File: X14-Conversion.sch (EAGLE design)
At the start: 13 parts, among them U1 LM2678SX-ADJ/NOPBTS7B

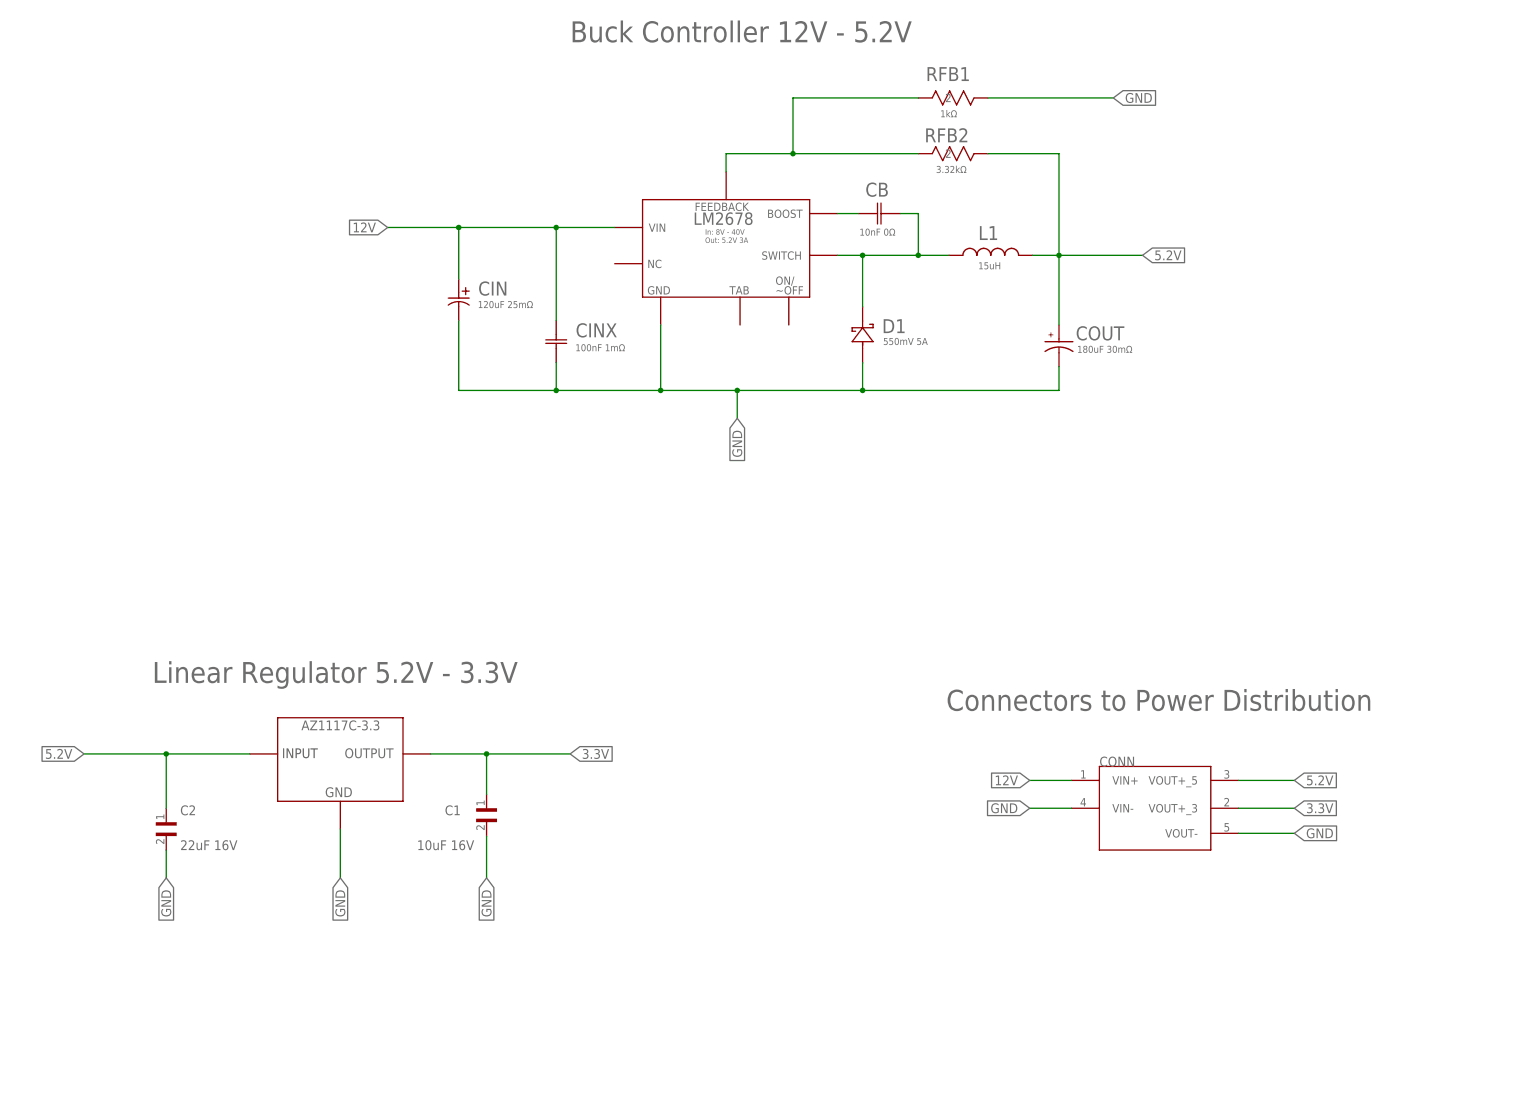
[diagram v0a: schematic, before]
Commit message: Fix Schematic, add test points, screw terminals and connectors
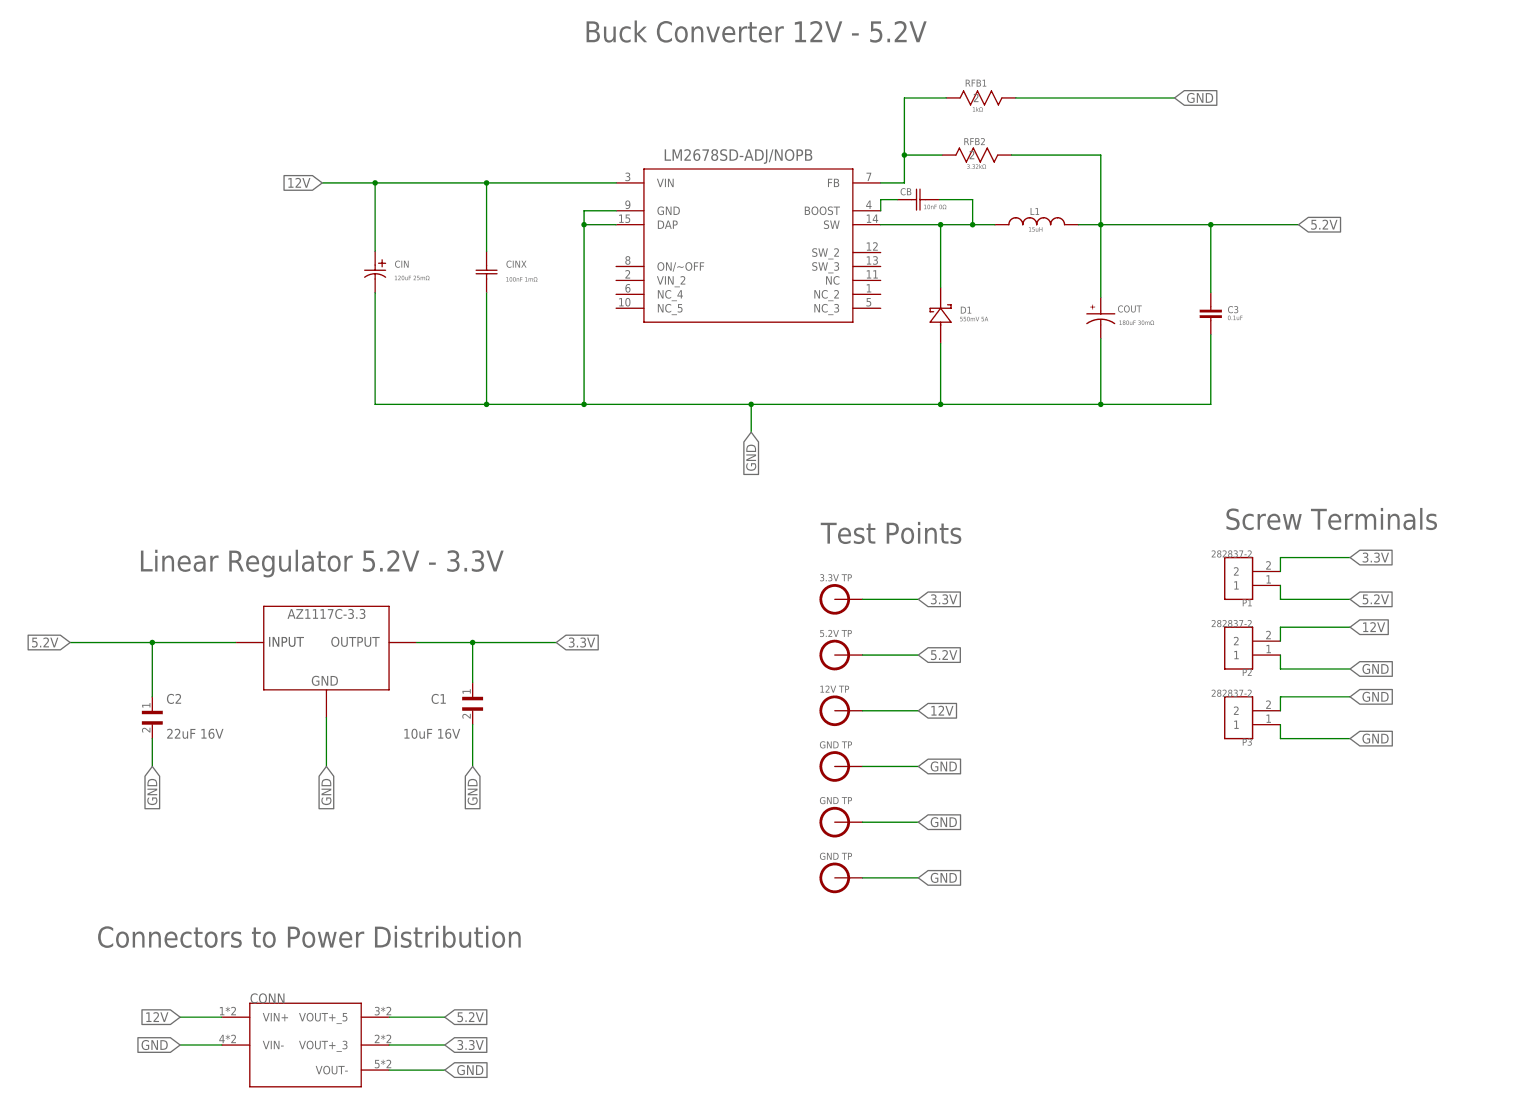
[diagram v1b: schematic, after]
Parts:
- removed U1: LM2678SX-ADJ/NOPBTS7B, LM2678SX-ADJNOPB:LM2678SX-ADJ/NOPBTS7B
- added C3: 0.1uF, SparkFun-Capacitors:0.1UF-0402-16V-10%
- added P1, P2, P3: 282837-2, ScrewPoints_282837-2:282837-2
- added U$2: 3.3V_TESTPOINT, testpoints:3.3V_TESTPOINT
- added U$3: 5.2V_TESTPOINT, testpoints:5.2V_TESTPOINT
- added U$4: 12V_TESTPOINT, testpoints:12V_TESTPOINT
- added U$5, U$6, U$7: GND_TESTPOINT, testpoints:GND_TESTPOINT
- added U2: LM2678SD-ADJ/NOPB, LM2678SX-ADJNOPB:LM2678SD-ADJ/NOPB
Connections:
- removed net N$1: RFB1.2, RFB2.2, U1.FEEDBACK
- removed net N$3: CB.2, D1.1, L1.1, U1.SWITCH_OUTPUT
- new net N$4: CB.1, U2.BOOST
- new net N$5: RFB1.2, RFB2.2, U2.FB
- net 12V: now also P2.2, U$4.12V, U2.VIN; no longer U1.VIN
- net 3.3V: now also P1.2, U$2.3.3V
- net 5.2V: now also C3.1, P1.1, U$3.5.2V
- net GND: now also C3.2, P2.1, P3.1, P3.2, U$5.GND, U$6.GND, U$7.GND, U2.DAP, U2.GND; no longer U1.GND
- net N$2: now also CB.2, D1.1, L1.1, U2.SW; no longer CB.1, U1.CB
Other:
- note added: "Buck Converter 12V - 5.2V"
- note added: "Screw Terminals"
- note added: "Test Points"
- note removed: "Buck Controller 12V - 5.2V"
- moved on the sheet: C1, C2, CB, CIN, CINX, CONN, COUT, D1, L1, RFB1, RFB2

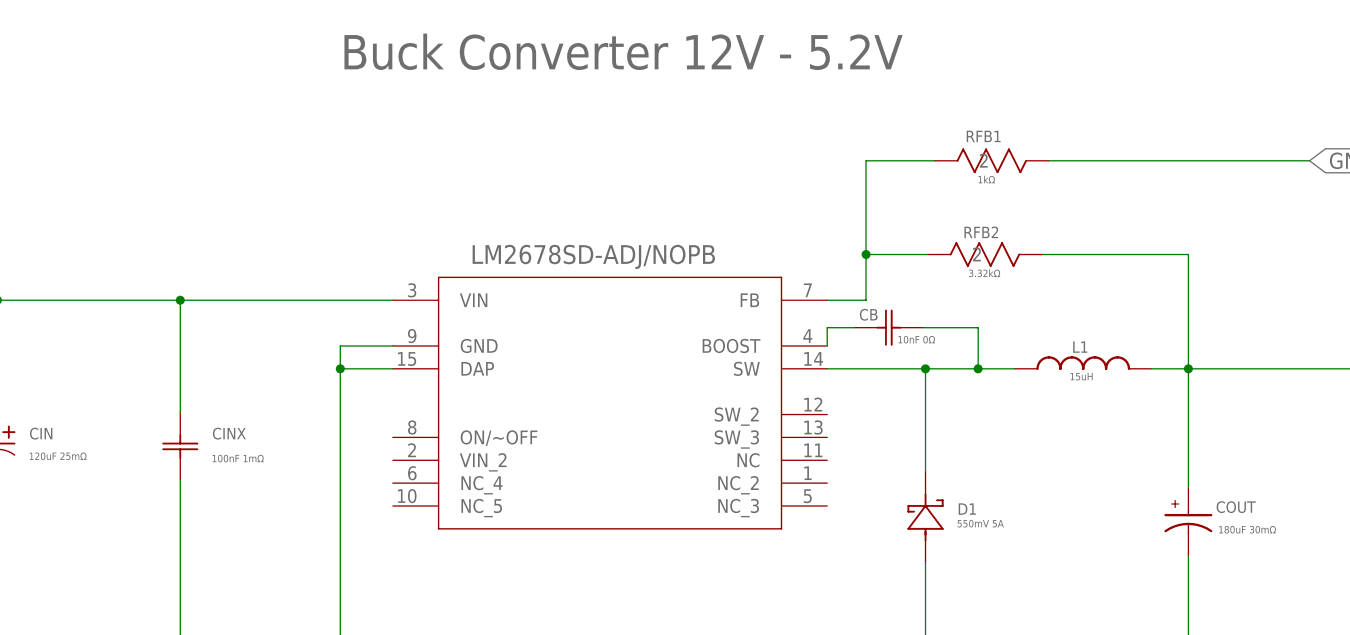
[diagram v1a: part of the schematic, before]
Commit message: Fix capacitors and resistors to Sparkfun components
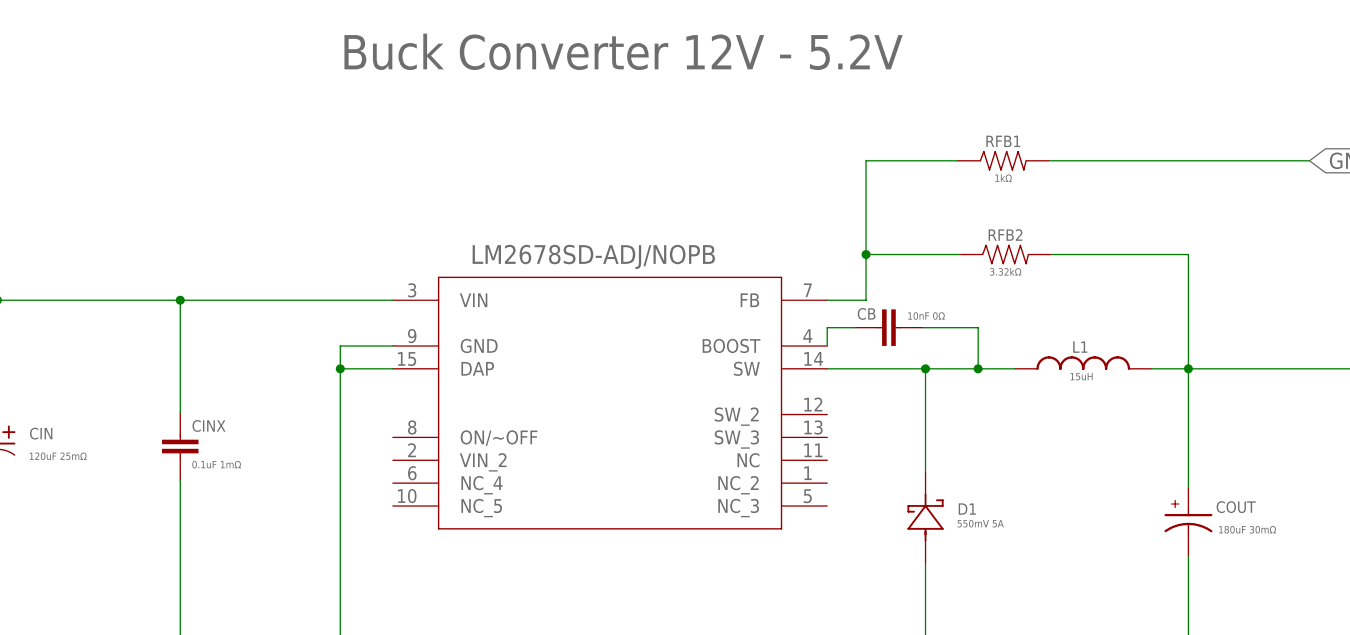
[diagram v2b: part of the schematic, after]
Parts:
- CB: device CGA4C2C0G1H103J060AA:CGA4C2C0G1H103J060AACAP_2012_TDK -> SparkFun-Capacitors:10NF-0603-50V-10%
- CINX: value 100nF 1mΩ -> 0.1uF 1mΩ; device GRM155R71C104KA88D:GRM155R71C104KA88DCAP_GRM_155_MUR -> SparkFun-Capacitors:0.1UF-0603-25V-(+80/-20%)
- RFB1: device CRCW04021K00FKED:CRCW04021K00FKEDRES_CRCW_0402 -> SparkFun-Resistors:1KOHM-0603-1/10W-1%
- RFB2: device CRCW04023K32FKED:CRCW04023K32FKEDRES_CRCW_0402 -> SparkFun-Resistors:3.3KOHM-0603-1/10W-1%
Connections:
- net 5.2V: now also RFB2.2; no longer RFB2.1
- net GND: now also RFB1.2; no longer RFB1.1
- net N$5: now also RFB1.1, RFB2.1; no longer RFB1.2, RFB2.2
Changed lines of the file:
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@@
 </classes>
 <parts>
-<part name="RFB1" library="CRCW04021K00FKED" deviceset="CRCW04021K00FKED" device="RES_CRCW_0402" value="1kΩ"/>
 <part name="D1" library="CDBC520-G_Library" deviceset="CDBC520-G" device="CDBC-G" value="550mV 5A"/>
 <part name="CIN" library="20SVPF120M" deviceset="20SVPF120M" device="PCAP_SVP_C6_PAN" value="120uF 25mΩ"/>
-<part name="RFB2" library="CRCW04023K32FKED" deviceset="CRCW04023K32FKED" device="RES_CRCW_0402" value="3.32kΩ"/>
 <part name="L1" library="IND, 15uH - hcma1305" deviceset="HCMA1305" device="" package3d_urn="urn:adsk.eagle:package:24201702/2" value="15uH"/>
-<part name="CB" library="CGA4C2C0G1H103J060AA" deviceset="CGA4C2C0G1H103J060AA" device="CAP_2012_TDK" value="10nF 0Ω"/>
 <part name="COUT" library="16SVP180MX" deviceset="16SVP180MX" device="" value="180uF 30mΩ"/>
-<part name="CINX" library="GRM155R71C104KA88D" deviceset="GRM155R71C104KA88D" device="CAP_GRM_155_MUR" value="100nF 1mΩ"/>
 <part name="FRAME1" library="frames" library_urn="urn:adsk.eagle:library:229" deviceset="A3L-LOC" device=""/>
 <part name="U$1" library="AZ1117C-3.3" deviceset="SOT150P410X160-3N" device=""/>
@@
 <part name="P3" library="ScrewPoints_282837-2" deviceset="282837-2" device=""/>
 <part name="C3" library="SparkFun-Capacitors" library_urn="urn:adsk.eagle:library:510" deviceset="0.1UF" device="-0402-16V-10%" package3d_urn="urn:adsk.eagle:package:37413/1" value="0.1uF"/>
+<part name="RFB2" library="SparkFun-Resistors" library_urn="urn:adsk.eagle:library:532" deviceset="3.3KOHM" device="-0603-1/10W-1%" package3d_urn="urn:adsk.eagle:package:39650/1" value="3.32kΩ"/>
+<part name="RFB1" library="SparkFun-Resistors" library_urn="urn:adsk.eagle:library:532" deviceset="1KOHM" device="-0603-1/10W-1%" package3d_urn="urn:adsk.eagle:package:39650/1" value="1kΩ"/>
+<part name="CB" library="SparkFun-Capacitors" library_urn="urn:adsk.eagle:library:510" deviceset="10NF" device="-0603-50V-10%" package3d_urn="urn:adsk.eagle:package:37414/1" value="10nF 0Ω"/>
+<part name="CINX" library="SparkFun-Capacitors" library_urn="urn:adsk.eagle:library:510" deviceset="0.1UF" device="-0603-25V-(+80/-20%)" package3d_urn="urn:adsk.eagle:package:37414/1" value="0.1uF 1mΩ"/>
 </parts>
 <sheets>
@@
 </plain>
 <instances>
-<instance part="RFB1" gate="A" x="38.1" y="88.9" smashed="yes">
-<attribute name="VALUE" x="42.8529" y="86.3981" size="0.8128" layer="96" ratio="10"/>
-<attribute name="NAME" x="41.5082" y="90.9701" size="1.27" layer="95" ratio="10"/>
-</instance>
 <instance part="D1" gate="A" x="37.084" y="54.356" smashed="yes" rot="R270">
 <attribute name="VALUE" x="40.5669" y="48.1711" size="0.8128" layer="96" ratio="10"/>
@@
 <attribute name="NAME" x="-62.5048" y="57.9501" size="1.27" layer="95" ratio="10"/>
 </instance>
-<instance part="RFB2" gate="A" x="37.338" y="78.486" smashed="yes">
-<attribute name="VALUE" x="41.8369" y="75.9841" size="0.8128" layer="96" ratio="10"/>
-<attribute name="NAME" x="41.2542" y="80.3021" size="1.27" layer="95" ratio="10"/>
-</instance>
 <instance part="L1" gate="G$1" x="46.99" y="65.786" smashed="yes">
 <attribute name="NAME" x="53.34" y="67.564" size="1.27" layer="95"/>
 <attribute name="VALUE" x="53.086" y="64.516" size="0.8128" layer="96"/>
 </instance>
-<instance part="CB" gate="A" x="29.21" y="70.358" smashed="yes">
-<attribute name="VALUE" x="33.9629" y="68.6181" size="0.8128" layer="96" ratio="10"/>
-<attribute name="NAME" x="29.6972" y="71.1581" size="1.27" layer="95" ratio="10"/>
-</instance>
 <instance part="COUT" gate="G$1" x="66.294" y="50.038" smashed="yes" rot="R270">
 <attribute name="NAME" x="69.342" y="49.784" size="1.27" layer="95"/>
 <attribute name="VALUE" x="69.596" y="47.498" size="0.8128" layer="96"/>
-</instance>
-<instance part="CINX" gate="A" x="-45.72" y="60.96" smashed="yes" rot="R270">
-<attribute name="VALUE" x="-42.2371" y="55.4101" size="0.8128" layer="96" ratio="10"/>
-<attribute name="NAME" x="-42.1848" y="57.9501" size="1.27" layer="95" ratio="10"/>
 </instance>
 <instance part="FRAME1" gate="G$1" x="-177.8" y="-116.84" smashed="yes">
@@
 <attribute name="VALUE" x="89.408" y="48.387" size="0.8128" layer="96"/>
 </instance>
+<instance part="RFB2" gate="G$1" x="45.974" y="78.486" smashed="yes">
+<attribute name="NAME" x="45.974" y="80.01" size="1.27" layer="95" align="bottom-center"/>
+<attribute name="VALUE" x="45.974" y="76.962" size="0.8128" layer="96" align="top-center"/>
+</instance>
+<instance part="RFB1" gate="G$1" x="45.72" y="88.9" smashed="yes">
+<attribute name="NAME" x="45.72" y="90.424" size="1.27" layer="95" align="bottom-center"/>
+<attribute name="VALUE" x="45.72" y="87.376" size="0.8128" layer="96" align="top-center"/>
+</instance>
+<instance part="CB" gate="G$1" x="34.29" y="70.358" smashed="yes" rot="R90">
+<attribute name="NAME" x="29.464" y="71.247" size="1.27" layer="95"/>
+<attribute name="VALUE" x="35.052" y="71.247" size="0.8128" layer="96"/>
+</instance>
+<instance part="CINX" gate="G$1" x="-45.72" y="55.88" smashed="yes">
+<attribute name="NAME" x="-44.45" y="58.801" size="1.27" layer="95"/>
+<attribute name="VALUE" x="-44.45" y="54.737" size="0.8128" layer="96"/>
+</instance>
 </instances>
 <busses>
@@
 <pinref part="COUT" gate="G$1" pin="2"/>
 <wire x1="66.294" y1="44.958" x2="66.294" y2="33.02" width="0.1524" layer="91"/>
-<pinref part="CINX" gate="A" pin="2"/>
 <wire x1="-45.72" y1="53.34" x2="-45.72" y2="33.02" width="0.1524" layer="91"/>
 <wire x1="-45.72" y1="33.02" x2="-27.94" y2="33.02" width="0.1524" layer="91"/>
@@
 <wire x1="86.36" y1="33.02" x2="86.36" y2="45.72" width="0.1524" layer="91"/>
 <junction x="66.294" y="33.02"/>
-</segment>
-<segment>
-<pinref part="RFB1" gate="A" pin="1"/>
+<pinref part="CINX" gate="G$1" pin="2"/>
+</segment>
+<segment>
 <wire x1="50.8" y1="88.9" x2="79.756" y2="88.9" width="0.1524" layer="91"/>
 <label x="79.756" y="88.9" size="1.778" layer="95" xref="yes"/>
+<pinref part="RFB1" gate="G$1" pin="2"/>
 </segment>
 <segment>
@@
 <pinref part="COUT" gate="G$1" pin="1"/>
 <wire x1="66.294" y1="52.578" x2="66.294" y2="65.786" width="0.1524" layer="91"/>
-<pinref part="RFB2" gate="A" pin="1"/>
-<wire x1="50.038" y1="78.486" x2="66.294" y2="78.486" width="0.1524" layer="91"/>
+<wire x1="51.054" y1="78.486" x2="66.294" y2="78.486" width="0.1524" layer="91"/>
 <wire x1="66.294" y1="78.486" x2="66.294" y2="65.786" width="0.1524" layer="91"/>
 <junction x="66.294" y="65.786"/>
@@
 <wire x1="86.36" y1="53.34" x2="86.36" y2="65.786" width="0.1524" layer="91"/>
 <junction x="86.36" y="65.786"/>
+<pinref part="RFB2" gate="G$1" pin="2"/>
 </segment>
 <segment>
@@
 <segment>
 <pinref part="U2" gate="A" pin="VIN"/>
-<pinref part="CINX" gate="A" pin="1"/>
 <wire x1="-22.098" y1="73.406" x2="-45.72" y2="73.406" width="0.1524" layer="91"/>
 <wire x1="-45.72" y1="73.406" x2="-45.72" y2="60.96" width="0.1524" layer="91"/>
@@
 <junction x="-66.04" y="73.406"/>
 <label x="-75.692" y="73.406" size="1.778" layer="95" rot="R180" xref="yes"/>
+<pinref part="CINX" gate="G$1" pin="1"/>
 </segment>
 <segment>
@@
 <pinref part="L1" gate="G$1" pin="1"/>
 <wire x1="26.162" y1="65.786" x2="37.084" y2="65.786" width="0.1524" layer="91"/>
-<pinref part="CB" gate="A" pin="2"/>
 <wire x1="37.084" y1="65.786" x2="42.926" y2="65.786" width="0.1524" layer="91"/>
 <wire x1="42.926" y1="65.786" x2="46.99" y2="65.786" width="0.1524" layer="91"/>
@@
 <wire x1="37.084" y1="54.356" x2="37.084" y2="65.786" width="0.1524" layer="91"/>
 <junction x="37.084" y="65.786"/>
+<pinref part="CB" gate="G$1" pin="2"/>
 </segment>
 </net>
@@
 <segment>
 <pinref part="U2" gate="A" pin="BOOST"/>
-<pinref part="CB" gate="A" pin="1"/>
 <wire x1="26.162" y1="68.326" x2="26.162" y2="70.358" width="0.1524" layer="91"/>
 <wire x1="26.162" y1="70.358" x2="29.21" y2="70.358" width="0.1524" layer="91"/>
+<pinref part="CB" gate="G$1" pin="1"/>
 </segment>
 </net>
@@
 <wire x1="26.162" y1="73.406" x2="30.48" y2="73.406" width="0.1524" layer="91"/>
 <wire x1="30.48" y1="73.406" x2="30.48" y2="78.486" width="0.1524" layer="91"/>
-<pinref part="RFB2" gate="A" pin="2"/>
-<wire x1="30.48" y1="78.486" x2="37.338" y2="78.486" width="0.1524" layer="91"/>
-<pinref part="RFB1" gate="A" pin="2"/>
+<wire x1="30.48" y1="78.486" x2="40.894" y2="78.486" width="0.1524" layer="91"/>
 <wire x1="30.48" y1="78.486" x2="30.48" y2="88.9" width="0.1524" layer="91"/>
-<wire x1="30.48" y1="88.9" x2="38.1" y2="88.9" width="0.1524" layer="91"/>
+<wire x1="30.48" y1="88.9" x2="40.64" y2="88.9" width="0.1524" layer="91"/>
 <junction x="30.48" y="78.486"/>
-</segment>
-</net>
+<pinref part="RFB1" gate="G$1" pin="1"/>
+<pinref part="RFB2" gate="G$1" pin="1"/>
+</segment>
+</net>
